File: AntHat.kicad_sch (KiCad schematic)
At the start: 76 parts, among them J1 Raspberry_Pi_2_3, J10 0353180420, J11 0353180420, J2 0455580003, J3 PSU Comm, J4 61900411021, J5 61900411021, J6 61900411021, J7 61900411021, J8 0353180420, J9 0353180420, Q1 DMP3013SFV-7, U1 AP64501SP-13, U2 EMC2305, U4 TPS54531DDAR

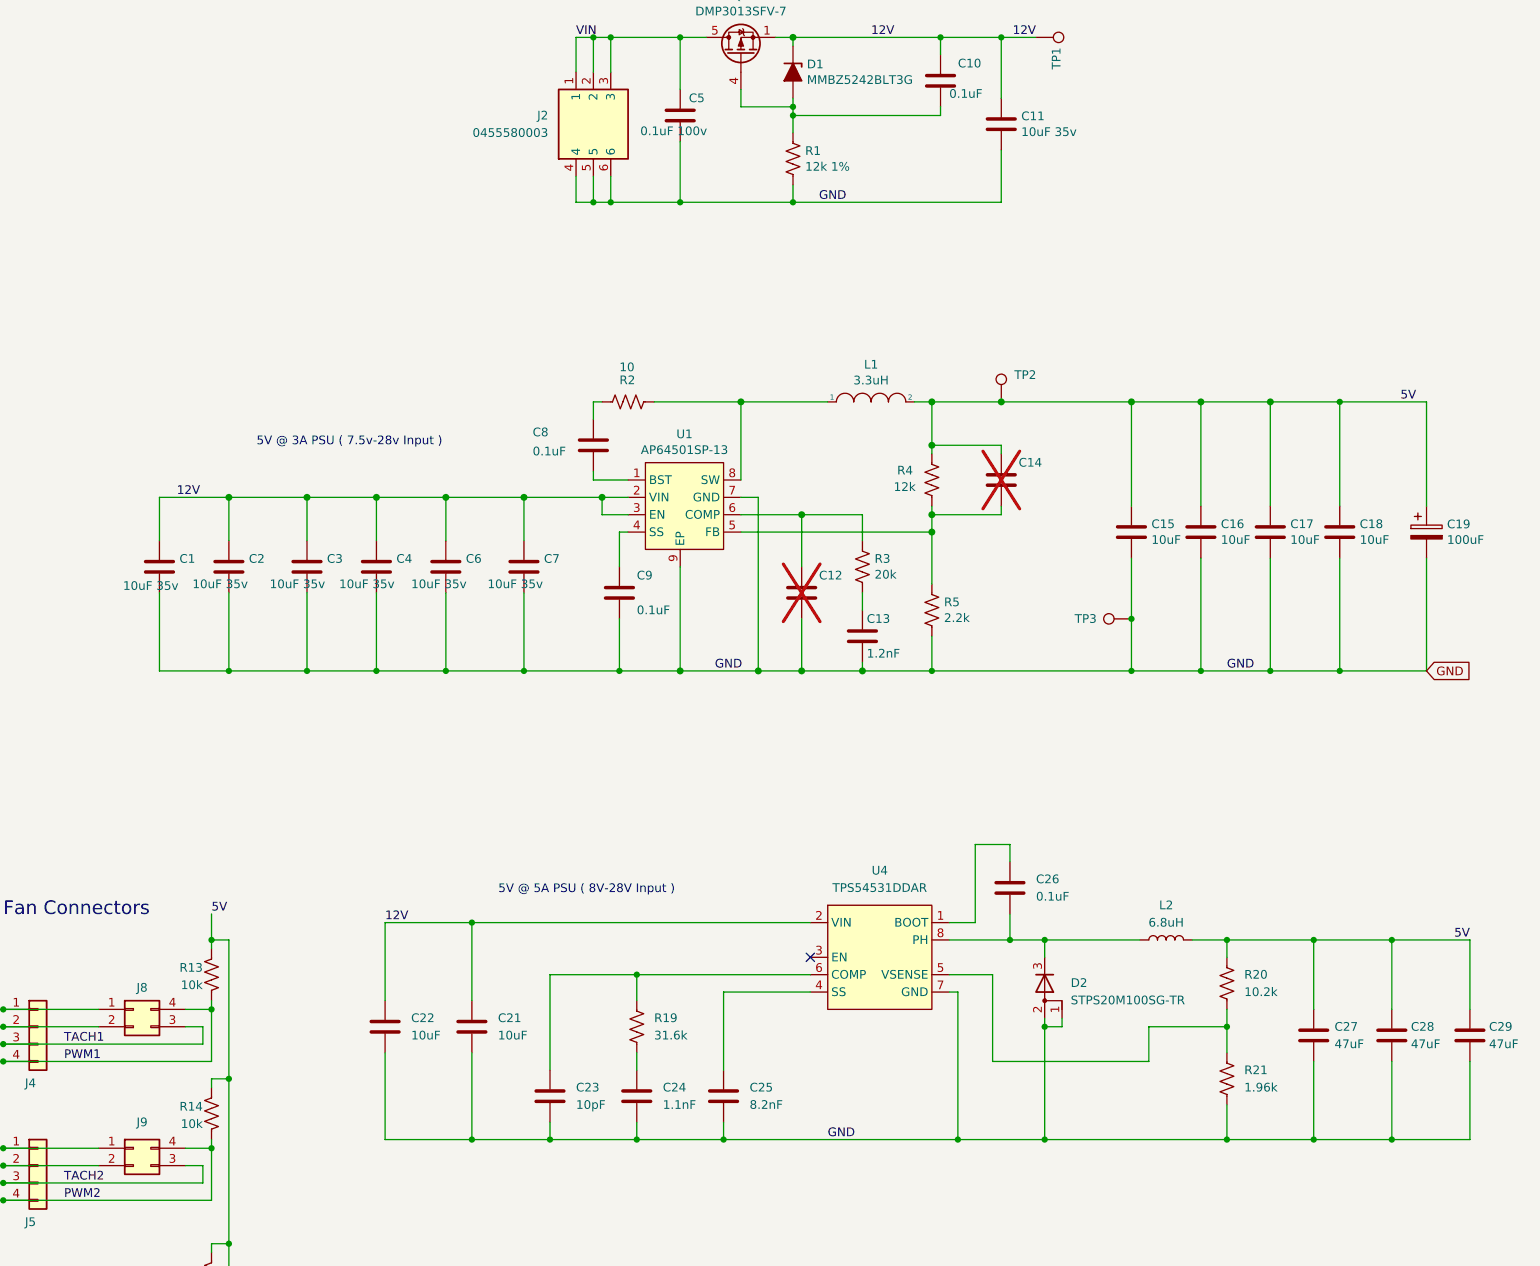
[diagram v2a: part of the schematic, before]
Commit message: deleted TPS54531. Changed OOS Inductor. DRC passes
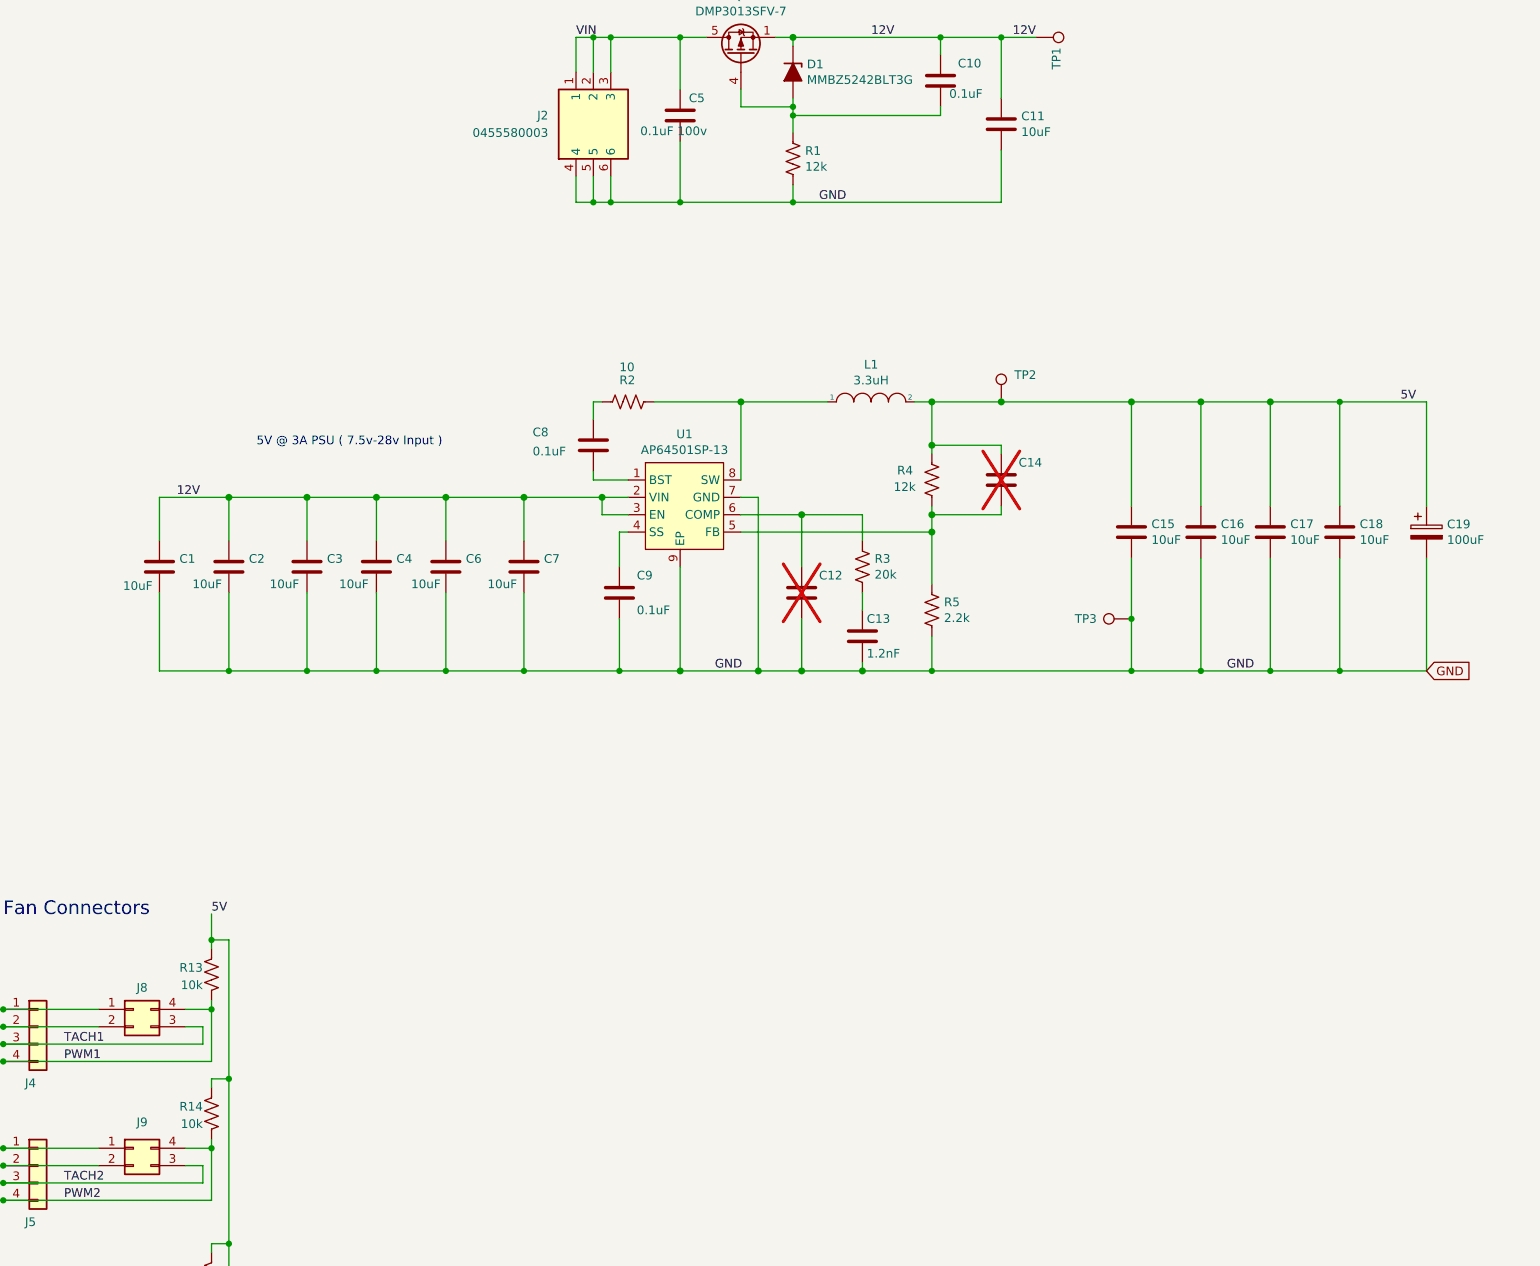
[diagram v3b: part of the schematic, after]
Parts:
- removed C21, C22: 10uF, Capacitor_SMD:C_1210_3225Metric, symbol Device:C
- removed C23: 10pF, Capacitor_SMD:C_0805_2012Metric, symbol Device:C
- removed C24: 1.1nF, Capacitor_SMD:C_0402_1005Metric, symbol Device:C
- removed C25: 8.2nF, Capacitor_SMD:C_0402_1005Metric, symbol Device:C
- removed C26: 0.1uF, Capacitor_SMD:C_0402_1005Metric, symbol Device:C
- removed C27, C28, C29: 47uF, Capacitor_SMD:C_1210_3225Metric, symbol Device:C
- removed D2: STPS20M100SG-TR, AntHat:D2PAK_L10.4-W8.5-P2.54-LS15.4-BR, symbol Device:D_AAK
- removed L2: 6.8uH, AntHat:IND_IHLP-4040DZ_VIS, symbol Device:L
- removed R19: 31.6k, Resistor_SMD:R_0402_1005Metric, symbol Device:R_US
- removed R20: 10.2k, Resistor_SMD:R_0402_1005Metric, symbol Device:R_US
- removed R21: 1.96k, Resistor_SMD:R_0402_1005Metric, symbol Device:R_US
- removed U4: TPS54531DDAR, AntHat:SOIC-8_L5.0-W4.0-P1.27-LS6.0-BL-EP2.0, symbol AntHat:TPS54531DDAR
- C1, C11, C2, C3, C4, C6, C7: value 10uF 35v -> 10uF; DK (none) -> 490-10505-1-ND; Field4 Digikey -> (none); Field5 490-10505-1-ND -> (none); Field6 GRM21BC8YA106KE11L -> (none); Field7 Murata -> (none); PARTNO (none) -> GRM21BC8YA106ME11L; Part Description 10uF 10% or 20% 35V Ceramic Capacitor X6S 0805 (2012 Metric) -> (none)
- C10, C8, C9: DK (none) -> 490-6328-1-ND; Field4 Farnell -> (none); Field5 2611911 -> (none); Field6 RM EMK105 B7104KV-F -> (none); Field7 TAIYO YUDEN EUROPE GMBH -> (none); Field8 110091611 -> (none); PARTNO (none) -> GRM155R71C104KA88J
- C13: Field4 Digikey -> (none); Field5 490-16429-1-ND -> (none); Field6 GCM155R71H122KA37D -> (none); Field7 Murata -> (none); Part Description 1200pF 10% 10V Ceramic Capacitor X5R 0402 (1005 Metric) -> (none)
- C14: Field4 Farnell -> (none); Field5 2666374 -> (none); Field6 GRM1555C1H221JA01D -> (none); Field7 Murata -> (none); Part Description 220 pF, 50 V, 0402 [1005 Metric], ± 5%, C0G / NP0/CH, GCM S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 -> (none)
- C15, C16, C17, C18: DK (none) -> 490-10505-1-ND; Field4 Digikey -> (none); Field5 490-14381-1-ND -> (none); Field6 GRM21BR71A106KA73L -> (none); Field7 Murata -> (none); Field8 111893011 -> (none); PARTNO (none) -> GRM21BC8YA106ME11L; Part Description 10uF 10% 10V Ceramic Capacitor X7R 0805 (2012 Metric) -> (none)
- C19: Field4 Mouser -> (none); Field5 667-EEF-CX0J101R -> (none); Part Description Capacitor, SP-Cap, 100u, 6.3V, 15mR ESR -> (none)
- C20: DK (none) -> 490-6328-1-ND; PARTNO (none) -> GRM155R71C104KA88J
- C5: DK (none) -> 490-10458-1-ND; Field4 Farnell -> (none); Field5 2611907 -> (none); Field6 GRM155R62A104KE14D -> (none); Field7 Murata -> (none); PARTNO (none) -> GRM155R62A104KE14D; Part Description 0.1uF 10% 100V Ceramic Capacitor X5R 0402 (1005 Metric) -> (none)
- H1, H2, H3, H4: Field4 nf -> (none); Field5 nf -> (none); Field6 nf -> (none); Field7 nf -> (none); Part Description M2.5 mounting hole -> (none)
- J1: DK (none) -> S7123-ND; PARTNO (none) -> PPPC202LFBN-RC
- L1: footprint Inductor_SMD:L_Bourns_SRN6045TA -> AntHat:IND-SMD_L5.7-W5.2; DK SRN6045TA-3R3YCT-ND -> SRP5030T-3R3MCT-ND; Field6 SRN6045TA-3R3Y -> (none); LCSC Part (none) -> C189931; PARTNO (none) -> SRP5030T-3R3M
- R1: value 12k 1% -> 12k; Field4 Farnell -> (none); Field5 9239367 -> (none); Field6 MCR01MZPF1202 -> (none); Field7 Rohm -> (none); Part Description Resistor 12K M1005 1% 63mW -> (none)
- R2: Field4 Farnell -> (none); Field5 9238999 -> (none); Field6 RC0402FR-0710RL -> (none); Field7 Yageo -> (none); Field8 URES00256 -> (none); Part Description Resistor 10R M1005 1% 63mW -> (none)
- R3: Field4 Farnell -> (none); Field5 2331485 -> (none); Field6 RK73H1ETTP2002F -> (none); Field7 KOA EUROPE GMBH -> (none); Part Description Resistor 20K M1005 1% 63mW -> (none)
- R4: Field4 Farnell -> (none); Field5 9239367 -> (none); Field6 MCR01MZPF1202 -> (none); Field7 Rohm -> (none); Part Description Resistor 12K M1005 1% 63mW -> (none)
- R5: Field4 Farnell -> (none); Field5 9239278 -> (none); Field6 RK73G1ETQTP2201D -> (none); Field7 KOA EUROPE GMBH -> (none); Field8 120889581 -> (none); Part Description Resistor 2.2K M1005 1% 63mW -> (none)
- TP1, TP2, TP3: Field4 nf -> (none); Field5 nf -> (none); Field6 nf -> (none); Field7 nf -> (none)
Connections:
- no-connect marks 3 -> 2
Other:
- note removed: "5V @ 5A PSU ( 8V-28V Input )"

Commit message: DRC, ERC and added gerbers
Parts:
- C13: value 1.2nF -> 1200pF; DK (none) -> 490-16429-1-ND; PARTNO (none) -> GCM155R71H122KA37D
- C19: DK (none) -> 478-3355-1-ND; PARTNO (none) -> TAJD107K010RNJ
- R1, R4: DK (none) -> 311-12.0KLRCT-ND; PARTNO (none) -> RC0402FR-0712KL
- R10, R11, R12, R9: DK (none) -> 311-36.0KLRCT-ND; PARTNO (none) -> RC0402FR-0736KL
- R13, R14, R15, R16: DK (none) -> 311-10.0KLRCT-ND; PARTNO (none) -> RC0402FR-0710KL
- R17, R18, R6: DK (none) -> 311-4.7KLRCT-ND; PARTNO (none) -> RC0402FR-074K7L
- R2: DK (none) -> 311-10.0LRCT-ND; PARTNO (none) -> RC0402FR-0710RL
- R3: DK (none) -> 311-20.0KLRCT-ND; PARTNO (none) -> RC0402FR-0720KL
- R5: DK (none) -> 311-2.20KLRCT-ND; PARTNO (none) -> RC0402FR-072K2L
- R7: DK (none) -> 311-33.0KLRCT-ND; PARTNO (none) -> RC0402FR-0733KL
- R8: DK (none) -> 311-22.0KLRCT-ND; PARTNO RMCF0805FT22K0 -> RC0402FR-0722KL
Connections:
- net +3.3v renamed 3V3
- no-connect marks 2 -> 28
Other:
- moved on the sheet: J10, J11, J4, J5, J6, J7, J8, J9, R13, R14, R15, R16
